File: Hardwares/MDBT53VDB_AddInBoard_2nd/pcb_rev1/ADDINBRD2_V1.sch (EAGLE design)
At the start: 21 parts, among them CN1 IF_4PIN, CN2 IF_4PIN, CN3 IF_2PIN, CN4 IF_2PIN, Q1 DMP2035UFDF-7, Q2 BC817-40QA, SW1 SKRPACE010, U1 SN74AHC1G00DRLR, U2 REF3325AIRSER, U3 MCP6232T-E/MNY

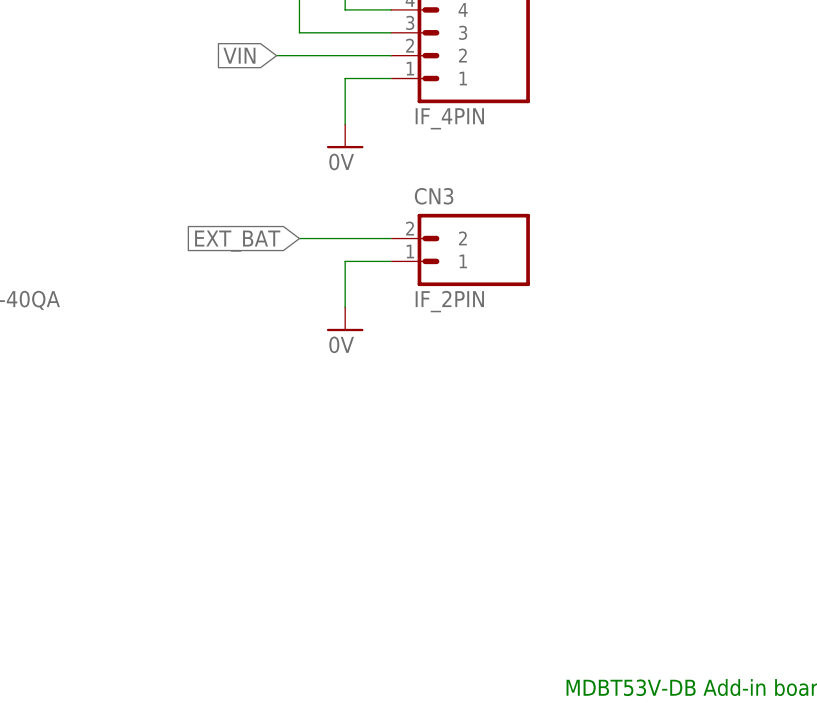
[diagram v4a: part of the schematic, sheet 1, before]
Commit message: 回路図を修正
・コメントを追加
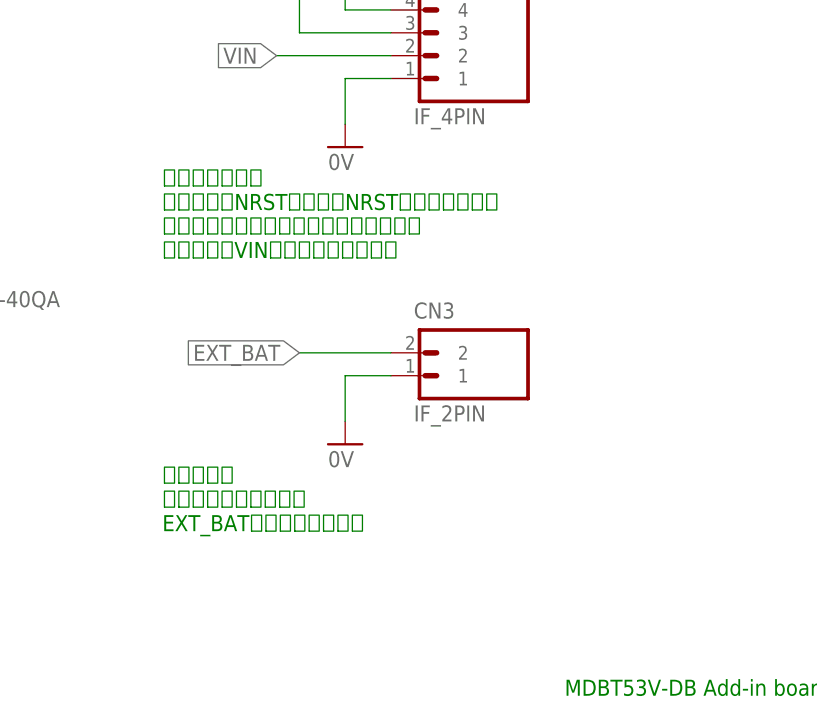
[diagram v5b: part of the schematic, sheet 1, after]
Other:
- note added: "リセット同期： ボード側のNRST端子を、NRSTに接続します。 ボード側でリセット実行した場合でも、 動作電源をVINに供給し続けます。"
- note added: "動作電源： 乾電池などの電源を、 EXT_BATから供給します。"
- note added: "動作電源： 電源電圧測定回路の動作電源を AVINに供給します。"
- note added: "基準電圧出力： 動作電源電圧の変化にかかわらず、 常に2.5Vを出力します。"
- note added: "測定対象電圧出力： 動作電源電圧を約75%に分圧した 電圧を出力します。"
- note added: "電源共有： 動作電源投入・遮断回路の VINをAVINとして利用します。"
- moved on the sheet: C3, CN3
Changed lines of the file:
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@@
 供給されなくなります。</text>
 <text x="175.26" y="124.46" size="2.54" layer="91" align="top-left">外部接続用端子</text>
+<text x="172.72" y="45.72" size="1.778" layer="91" align="top-left">動作電源：
+乾電池などの電源を、
+EXT_BATから供給します。</text>
+<text x="172.72" y="78.74" size="1.778" layer="91" align="top-left">リセット同期：
+ボード側のNRST端子を、NRSTに接続します。
+ボード側でリセット実行した場合でも、
+動作電源をVINに供給し続けます。</text>
 </plain>
 <instances>
@@
 <instance part="U1" gate="G$1" x="99.06" y="66.04"/>
 <instance part="CN2" gate="G$1" x="198.12" y="96.52"/>
-<instance part="CN3" gate="G$1" x="198.12" y="71.12"/>
-<instance part="GND12" gate="1" x="193.04" y="60.96"/>
+<instance part="CN3" gate="G$1" x="198.12" y="58.42"/>
+<instance part="GND12" gate="1" x="193.04" y="48.26"/>
 <instance part="GND13" gate="1" x="193.04" y="81.28"/>
 </instances>
@@
 <pinref part="CN3" gate="G$1" pin="1"/>
 <pinref part="GND12" gate="1" pin="0V"/>
-<wire x1="198.12" y1="68.58" x2="193.04" y2="68.58" width="0.1524" layer="91"/>
-<wire x1="193.04" y1="68.58" x2="193.04" y2="63.5" width="0.1524" layer="91"/>
+<wire x1="198.12" y1="55.88" x2="193.04" y2="55.88" width="0.1524" layer="91"/>
+<wire x1="193.04" y1="55.88" x2="193.04" y2="50.8" width="0.1524" layer="91"/>
 </segment>
 <segment>
@@
 <segment>
 <pinref part="CN3" gate="G$1" pin="2"/>
-<wire x1="198.12" y1="71.12" x2="187.96" y2="71.12" width="0.1524" layer="91"/>
-<label x="187.96" y="71.12" size="1.778" layer="95" rot="R180" xref="yes"/>
+<wire x1="198.12" y1="58.42" x2="187.96" y2="58.42" width="0.1524" layer="91"/>
+<label x="187.96" y="58.42" size="1.778" layer="95" rot="R180" xref="yes"/>
 </segment>
 </net>
@@
 <text x="144.78" y="142.24" size="2.54" layer="91" align="top-left">電圧入力バッファ</text>
 <text x="48.26" y="53.34" size="2.54" layer="91" align="top-left">外部接続用端子</text>
+<text x="114.3" y="45.72" size="1.778" layer="91" align="top-left">電源共有：
+動作電源投入・遮断回路の
+VINをAVINとして利用します。
+</text>
+<text x="193.04" y="71.12" size="1.778" layer="91" align="top-left">動作電源：
+電源電圧測定回路の動作電源を
+AVINに供給します。</text>
+<text x="193.04" y="91.44" size="1.778" layer="91" align="top-left">基準電圧出力：
+動作電源電圧の変化にかかわらず、
+常に2.5Vを出力します。</text>
+<text x="193.04" y="116.84" size="1.778" layer="91" align="top-left">測定対象電圧出力：
+動作電源電圧を約75%に分圧した
+電圧を出力します。</text>
 </plain>
 <instances>
@@
 <instance part="R4" gate="G$1" x="78.74" y="127"/>
 <instance part="R5" gate="G$1" x="106.68" y="127"/>
-<instance part="C3" gate="G$1" x="175.26" y="71.12"/>
+<instance part="C3" gate="G$1" x="175.26" y="68.58"/>
 <instance part="U3" gate="G$1" x="170.18" y="109.22"/>
 <instance part="GND9" gate="1" x="175.26" y="106.68"/>
-<instance part="GND11" gate="1" x="175.26" y="58.42"/>
+<instance part="GND11" gate="1" x="175.26" y="55.88"/>
 <instance part="CN1" gate="G$1" x="76.2" y="30.48"/>
 <instance part="GND10" gate="1" x="71.12" y="15.24"/>
@@
 <pinref part="GND11" gate="1" pin="0V"/>
 <pinref part="C3" gate="G$1" pin="2"/>
-<wire x1="175.26" y1="60.96" x2="175.26" y2="66.04" width="0.1524" layer="91"/>
+<wire x1="175.26" y1="58.42" x2="175.26" y2="63.5" width="0.1524" layer="91"/>
 </segment>
 <segment>
@@
 <segment>
 <pinref part="C3" gate="G$1" pin="1"/>
-<wire x1="175.26" y1="73.66" x2="175.26" y2="78.74" width="0.1524" layer="91"/>
-<wire x1="175.26" y1="78.74" x2="195.58" y2="78.74" width="0.1524" layer="91"/>
-<label x="195.58" y="78.74" size="1.778" layer="95" xref="yes"/>
-</segment>
-<segment>
+<wire x1="175.26" y1="71.12" x2="175.26" y2="76.2" width="0.1524" layer="91"/>
+<wire x1="175.26" y1="76.2" x2="195.58" y2="76.2" width="0.1524" layer="91"/>
+<label x="195.58" y="76.2" size="1.778" layer="95" xref="yes"/>
+</segment>
+<segment>
